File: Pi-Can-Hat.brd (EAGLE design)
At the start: 55.2 x 64.8 mm, 51 parts, among them IC1 MCP2515-I/SO, IC2 MCP2562-E/SN, IC3 MCP2515-I/SO, IC4 MCP2562-E/SN, IC5 MEGA8-AI, J1 RJ45 CAN.Bus, Q1 16MHz, Q2 IRF7410, Q3 16MHz, Q4 16MHz, U1 TSR 2-2450

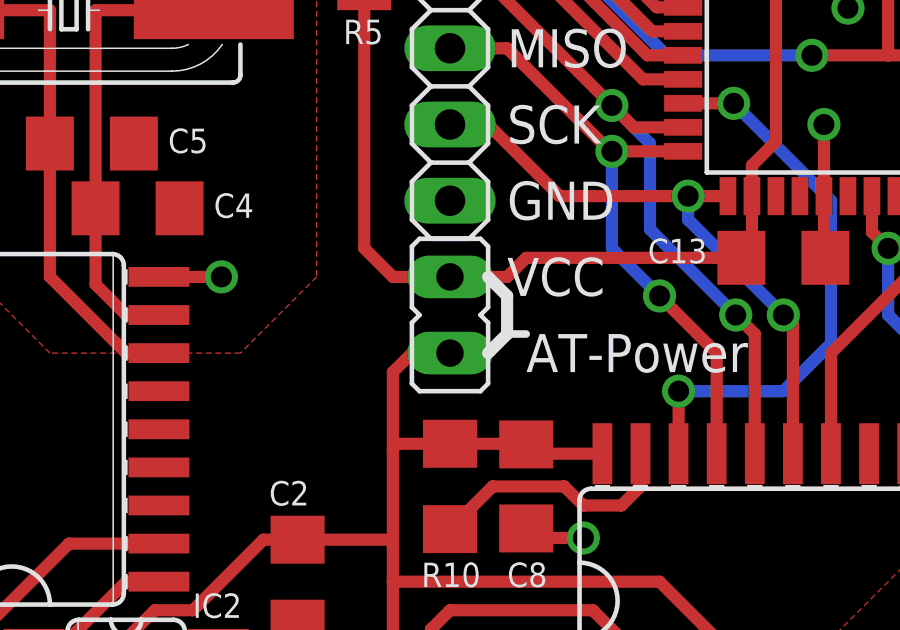
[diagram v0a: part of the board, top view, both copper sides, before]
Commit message: Zusätzliche Kondensatoren auf CAN-Hat gegen Reset beim Einschalten des Pis
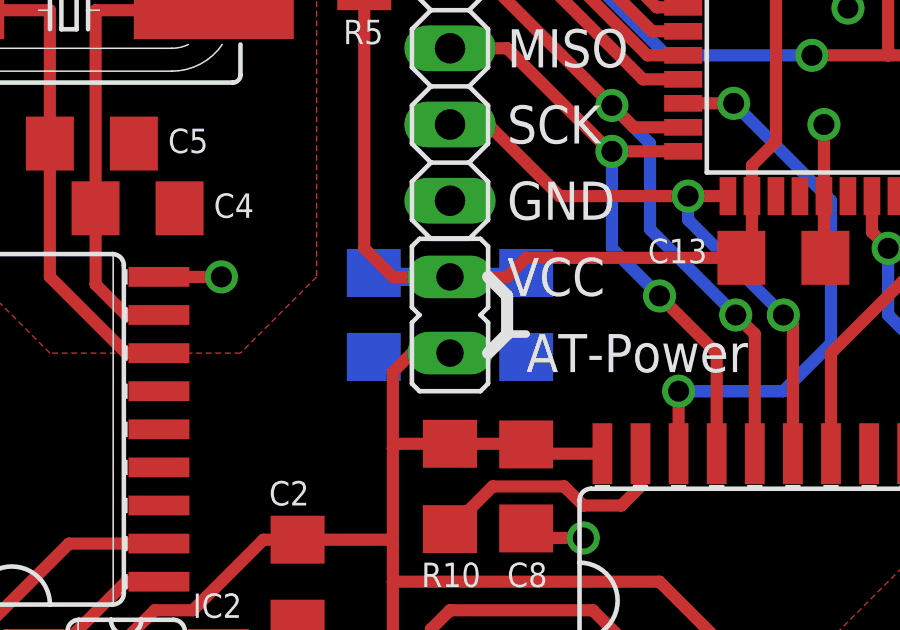
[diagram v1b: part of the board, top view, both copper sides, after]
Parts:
- added C16, C17: 10µF/25V, rcl:C1206
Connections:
- net AT_VCC: now also C16.1, C17.1
- net GND: now also C16.2, C17.2
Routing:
- net AT_VCC: track 36.4 -> 41.7 mm
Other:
- board text added: "Rev 2019/08 (c) Peter Müller"
- board text removed: "Rev 2019/05 (c) Peter Müller"
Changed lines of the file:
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@@
 <text x="26.67" y="10.795" size="1.778" layer="25" font="vector" ratio="15" rot="R270" align="center">HomePi
 CAN-Hat</text>
-<text x="50.8" y="25.4" size="1.778" layer="26" font="vector" ratio="15" rot="SMR270" align="center">Rev 2019/05
+<text x="50.8" y="25.4" size="1.778" layer="26" font="vector" ratio="15" rot="SMR270" align="center">Rev 2019/08
 (c) Peter Müller</text>
 <text x="35.56" y="19.685" size="1.27" layer="25" font="vector" ratio="10" align="top-center">+5V</text>
@@
 <attribute name="VALUE" x="45.085" y="59.055" size="1.27" layer="27"/>
 </element>
+<element name="C16" library="rcl" package="C1206" value="10µF/25V" x="24.13" y="38.735" smashed="yes" rot="MR270">
+<attribute name="NAME" x="24.13" y="41.275" size="0.8128" layer="26" font="vector" rot="MR0" align="bottom-center"/>
+<attribute name="VALUE" x="26.67" y="40.005" size="1.27" layer="28" rot="MR270"/>
+</element>
+<element name="C17" library="rcl" package="C1206" value="10µF/25V" x="29.21" y="38.735" smashed="yes" rot="MR270">
+<attribute name="NAME" x="29.21" y="41.275" size="0.8128" layer="26" font="vector" rot="MR0" align="bottom-center"/>
+<attribute name="VALUE" x="31.75" y="40.005" size="1.27" layer="28" rot="MR270"/>
+</element>
 </elements>
 <signals>
@@
 <vertex x="6.0325" y="61.2775"/>
 </polygon>
+<contactref element="C17" pad="2"/>
+<contactref element="C16" pad="2"/>
 </signal>
 <signal name="GPIO.06">
@@
 <wire x1="23.8125" y1="40.9575" x2="24.765" y2="40.005" width="0.4064" layer="1"/>
 <wire x1="24.765" y1="40.005" x2="26.67" y2="40.005" width="0.4064" layer="1"/>
+<contactref element="C16" pad="1"/>
+<contactref element="C17" pad="1"/>
+<wire x1="24.13" y1="40.135" x2="24.13" y2="40.005" width="0.6096" layer="16"/>
+<wire x1="24.13" y1="40.005" x2="26.67" y2="40.005" width="0.6096" layer="16"/>
+<wire x1="29.21" y1="40.135" x2="29.21" y2="40.005" width="0.6096" layer="16"/>
+<wire x1="29.21" y1="40.005" x2="26.67" y2="40.005" width="0.6096" layer="16"/>
 </signal>
 <signal name="!PI_ON">
